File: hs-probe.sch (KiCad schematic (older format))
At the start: 52 parts, among them J1 USB_C_Receptacle_USB2.0, J2 Castellated Vias, J3 Castellated Vias, J4 Castellated Vias, U1 STM32F723IEKx, U2 DSC6003HI2A-012.0000T, U3 MIC5259, U4 NUF8401MNT4G, U5 STDC14, U6 SOICbite_SWD, U7 MIC5259, U8 USB3740B-AI9

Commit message: Updated design from review comment
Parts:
- added R9: 1k, passive:R_0402, symbol Device:R_Small
- J4: footprint connectors:1x4_1.5mm_castellated -> connectors:1x3_1.5mm_castellated; symbol Connector:Conn_01x04_Female -> Connector:Conn_01x03_Female
- U3, U7: value MIC5259 -> MIC5353; footprint dfn:DFN-6-1EP_2x2mm_P0.65mm_EP1x1.6mm -> dfn:DFN-6-1EP_1.6x1.6mm_P0.5mm_EP0.5x1.26mm; MPN MIC5259-3.3YML-TR -> MIC5353-3.3YMT
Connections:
- net labels added: FS_VBUS, HS_VBUS
- net labels removed: T_VCC_PWR
- wire segments 239 -> 246
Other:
- note added: "DESIGN NOTE:\nT_VCC is read before \nenabling 3.3V power."
- note removed: "DESIGN NOTE:\nT_VCC is not read, this assumes\nthat the target is running at the\nsame voltage as the probe."
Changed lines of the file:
@@
 	10000 1050 10000 650
 Text Notes 14200 1150 0    50   ~ 0
-DESIGN NOTE:\nT_VCC is not read, this assumes\nthat the target is running at the\nsame voltage as the probe.
+DESIGN NOTE:\nT_VCC is read before \nenabling 3.3V power.
 Wire Notes Line
-	14150 750  15500 750
+	14150 850  15050 850
 Wire Notes Line
-	15500 750  15500 1200
+	15050 850  15050 1200
 Wire Notes Line
-	15500 1200 14150 1200
+	15050 1200 14150 1200
 Wire Notes Line
-	14150 1200 14150 750
+	14150 1200 14150 850
 Text Label 14100 3650 2    50   ~ 0
 NRST
@@
 P 13000 7750
 F 0 "U3" H 13250 7915 50  0000 C CNN
-F 1 "MIC5259" H 13250 7824 50  0000 C CNN
-F 2 "dfn:DFN-6-1EP_2x2mm_P0.65mm_EP1x1.6mm" H 13000 7750 50  0001 C CNN
-F 3 "http://ww1.microchip.com/downloads/en/DeviceDoc/mic5259.pdf" H 13000 7750 50  0001 C CNN
-F 4 "MIC5259-3.3YML-TR" H 13000 7750 50  0001 C CNN "MPN"
+F 1 "MIC5353" H 13250 7824 50  0000 C CNN
+F 2 "dfn:DFN-6-1EP_1.6x1.6mm_P0.5mm_EP0.5x1.26mm" H 13000 7750 50  0001 C CNN
+F 3 "https://ww1.microchip.com/downloads/en/DeviceDoc/mic5353.pdf" H 13000 7750 50  0001 C CNN
+F 4 "MIC5353-3.3YMT" H 13000 7750 50  0001 C CNN "MPN"
 	1    13000 7750
 	1    0    0    -1
@@
 P 13000 8500
 F 0 "U7" H 13250 8665 50  0000 C CNN
-F 1 "MIC5259" H 13250 8574 50  0000 C CNN
-F 2 "dfn:DFN-6-1EP_2x2mm_P0.65mm_EP1x1.6mm" H 13000 8500 50  0001 C CNN
-F 3 "http://ww1.microchip.com/downloads/en/DeviceDoc/mic5259.pdf" H 13000 8500 50  0001 C CNN
-F 4 "MIC5259-3.3YML-TR" H 13000 8500 50  0001 C CNN "MPN"
+F 1 "MIC5353" H 13250 8574 50  0000 C CNN
+F 2 "dfn:DFN-6-1EP_1.6x1.6mm_P0.5mm_EP0.5x1.26mm" H 13000 8500 50  0001 C CNN
+F 3 "https://ww1.microchip.com/downloads/en/DeviceDoc/mic5353.pdf" H 13000 8500 50  0001 C CNN
+F 4 "MIC5353-3.3YMT" H 13000 8500 50  0001 C CNN "MPN"
 	1    13000 8500
 	1    0    0    -1
@@
 T_VCC_EN
 Text Label 14050 8600 0    50   ~ 0
-T_VCC_PWR
+T_VCC
 Text Label 13050 1100 2    50   ~ 0
 T_VCC
@@
 	7900 8700 7800 8700
 Text Label 13050 1000 2    50   ~ 0
-T_VCC_PWR
+T_VCC
 Wire Wire Line
 	13050 1000 13150 1000
@@
 $EndComp
 $Comp
-L Connector:Conn_01x04_Female J4
+L Connector:Conn_01x03_Female J4
 U 1 1 5F14F2FD
 P 13700 6000
-F 0 "J4" H 13592 5575 50  0000 C CNN
-F 1 "Castellated Vias" H 13592 5666 50  0000 C CNN
-F 2 "connectors:1x4_1.5mm_castellated" H 13700 6000 50  0001 C CNN
+F 0 "J4" H 13592 5675 50  0000 C CNN
+F 1 "Castellated Vias" H 13592 5766 50  0000 C CNN
+F 2 "connectors:1x3_1.5mm_castellated" H 13700 6000 50  0001 C CNN
 F 3 "~" H 13700 6000 50  0001 C CNN
 	1    13700 6000
@@
 Text Label 13400 4600 2    50   ~ 0
 T_TDI
-Text Label 13400 5800 2    50   ~ 0
-T_VCC
 Wire Wire Line
 	13400 5900 13500 5900
 Text Label 13400 5900 2    50   ~ 0
-T_VCC_PWR
-Wire Wire Line
-	13400 5800 13500 5800
+T_VCC
 Wire Wire Line
 	13400 5350 13500 5350
@@
 Wire Wire Line
 	7900 8000 7800 8000
+Text Label 7900 2800 0    50   ~ 0
+FS_VBUS
+Wire Wire Line
+	7900 2800 7800 2800
+Text Label 7900 4900 0    50   ~ 0
+HS_VBUS
+Wire Wire Line
+	7900 4900 7800 4900
+$Comp
+L Device:R_Small R9
+U 1 1 5F1A949A
+P 9600 2850
+F 0 "R9" V 9404 2850 50  0000 C CNN
+F 1 "1k" V 9495 2850 50  0000 C CNN
+F 2 "passive:R_0402" H 9600 2850 50  0001 C CNN
+F 3 "~" H 9600 2850 50  0001 C CNN
+F 4 "1%" H 9600 2850 50  0001 C CNN "Tolerance"
+	1    9600 2850
+	0    1    1    0
+$EndComp
+$Comp
+L power:+5V #PWR038
+U 1 1 5F1A9A32
+P 9850 2850
+F 0 "#PWR038" H 9850 2700 50  0001 C CNN
+F 1 "+5V" H 9865 3023 50  0000 C CNN
+F 2 "" H 9850 2850 50  0001 C CNN
+F 3 "" H 9850 2850 50  0001 C CNN
+	1    9850 2850
+	0    1    1    0
+$EndComp
+Wire Wire Line
+	9850 2850 9700 2850
+Wire Wire Line
+	9500 2850 9400 2850
+Wire Wire Line
+	9400 2850 9400 2750
+Wire Wire Line
+	9400 2750 9300 2750
+Wire Wire Line
+	9400 2950 9300 2950
+Wire Wire Line
+	9400 2850 9400 2950
+Connection ~ 9400 2850
+Text Label 9300 2750 2    50   ~ 0
+FS_VBUS
+Text Label 9300 2950 2    50   ~ 0
+HS_VBUS
 $EndSCHEMATC

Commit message: Major schematic cleanup
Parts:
- removed U1: STM32F723IEKx, bga:UFBGA-201_10x10mm_Layout15x15_P0.65mm, symbol MCU_ST_STM32F7:STM32F723IEKx
- added U1: hs-probe-stm32, bga:UFBGA-201_10x10mm_Layout15x15_P0.65mm, symbol hs-probe-stm32:hs-probe-stm32
- U2: value DSC6003HI2A-012.0000T -> 12 MHz
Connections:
- net +3V3: now also U1.C1 (VBAT), U1.C5 (VDD[12]), U1.C6 (PDR_ON), U1.C7 (VDD[12]), U1.C8 (VDDSDMMC), U1.C9 (VDD[12]), U1.F3 (VDD[12]), U1.G13 (VDD[12]), U1.G3 (VDD[12]), U1.H13 (VDDUSB), U1.J12 (VDD[12]), U1.J13 (VDD[12]), U1.K4 (VDD[12]), U1.N10 (VDD[12]), U1.N8 (VDD[12]), U1.N9 (VDD[12]), U1.P1 (VREF+), U1.R1 (VDDA)
- net BOOT0: now also U1.D6 (BOOT0)
- net D_FS_N: now also U1.C15 (PA11/USB_OTG_FS_DM)
- net D_FS_P: now also U1.B15 (PA12/USB_OTG_FS_DP)
- net D_HS_N: now also U1.R14 (PB14/USB_OTG_HS_DM)
- net D_HS_P: now also U1.R15 (PB15/USB_OTG_HS_DP)
- net FS_VBUS: now also U1.E15 (PA9/USB_OTG_FS_VBUS), U1.P13 (PB13/USB_OTG_HS_VBUS)
- net GND: now also U1.D5 (VSS[36]), U1.D7 (VSS[36]), U1.D8 (VSS[36]), U1.D9 (VSS[36]), U1.F10 (VSS[36]), U1.F12 (VSS[36]), U1.F2 (VSS[36]), U1.F6 (VSS[36]), U1.F7 (VSS[36]), U1.F8 (VSS[36]), U1.F9 (VSS[36]), U1.G10 (VSS[36]), U1.G12 (VSS[36]), U1.G2 (VSS[36]), U1.G6 (VSS[36]), U1.G7 (VSS[36]), U1.G8 (VSS[36]), U1.G9 (VSS[36]), U1.H10 (VSS[36]), U1.H12 (VSS[36]), U1.H6 (VSS[36]), U1.H7 (VSS[36]), U1.H8 (VSS[36]), U1.H9 (VSS[36]), U1.J10 (VSS[36]), U1.J6 (VSS[36]), U1.J7 (VSS[36]), U1.J8 (VSS[36]), U1.J9 (VSS[36]), U1.K10 (VSS[36]), U1.K6 (VSS[36]), U1.K7 (VSS[36]), U1.K8 (VSS[36]), U1.K9 (VSS[36]), U1.L4 (BYPASS_REG), U1.M1 (VSSA), U1.M8 (VSS[36]), U1.M9 (VSS[36]), U1.N1 (VREF-)
- net GNDDetect: now also U1.A7 (PG14/GNDDet)
- net GPIO1: now also U1.P15 (PD8/GPIO1)
- net GPIO2: now also U1.N15 (PD10/GPIO2)
- net LED1: now also U1.B14 (PC10/LED1)
- net LED2: now also U1.A5 (PB8/LED2)
- net LED3: now also U1.A4 (PE0/LED3)
- net NRST: now also U1.J1 (NRST)
- net OSC: now also U1.G1 (PH0-OSC_IN/RCC_OSC_IN)
- net P_SWCLK: now also U1.A14 (PA14/SYS_JTCK-SWCLK)
- net P_SWDIO: now also U1.A15 (PA13/SYS_JTMS-SWDIO)
- net RESET: now also U1.A8 (PG13/RESET)
- net RPHY: now also U1.J15 (REXTPHYHS)
- net SPI1_CLK: now also U1.A10 (PB3/SPI1_SCK), U1.D14 (PI1/SPI2_SCK)
- net SPI1_MISO: now also U1.A6 (PB5/SPI1_MOSI), U1.A9 (PB4/SPI1_MISO)
- net SPI2_MISO: now also U1.B5 (PB7/USART1_RX), U1.C14 (PI2/SPI2_MISO)
- net SPI2_MOSI: now also U1.C13 (PI3/SPI2_MOSI)
- net T_VCC_EN: now also U1.A2 (PE2/T_VCC_EN)
- net T_VCC_MEAS: now also U1.R2 (PA3/ADC1_IN3)
- net USART1_TX: now also U1.B6 (PB6/USART1_TX)
- net USART2_RX: now also U1.B11 (PD6/USART2_RX)
- net USART2_TX: now also U1.C11 (PD5/USART2_TX)
- net USB_SEL: now also U1.R12 (PB10/USB_SEL)
- net V12PHY: now also U1.J14 (V12PHYHS)
- net VCAP1: now also U1.M10 (VCAP_1)
- net VCAP2: now also U1.F13 (VCAP_2)
- no-connect marks 7 -> 86
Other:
- note added: "Board-edge castellated vias"
- note added: "DESIGN NOTE:\nOn startup the FS port is connected for access to the \nSTM32 USB bootloader. The firmware can then switch \nover to the HS port."
- note added: "Designed by: Emil Fresk\nTwitter / Github: @korken89\nLink: https://github.com/korken89/hs-probe"
- note added: "MCU I/O"
- note added: "MCU Power, Config and Clock"
- note added: "Probe power and optional target power"
- note added: "Target SWD/JTAG port with ESD protection"
- note added: "USB-C port with USB MUX"
- moved on the sheet: C1, C10, C11, C12, C13, C14, C15, C16, C17, C18, C19, C2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

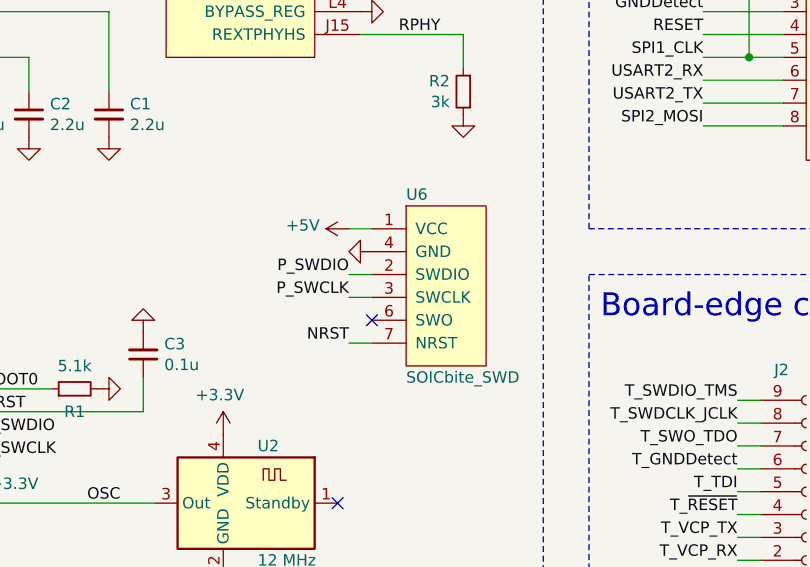
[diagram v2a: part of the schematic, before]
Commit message: Moved to tag connect
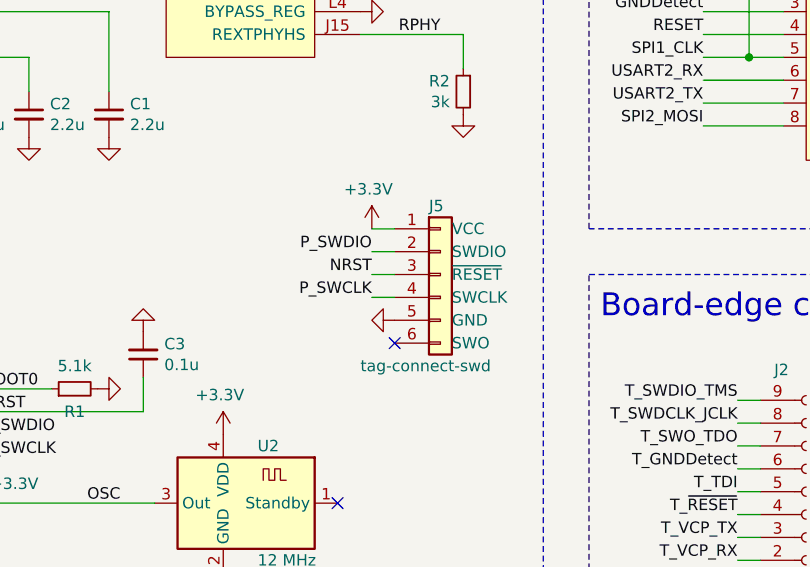
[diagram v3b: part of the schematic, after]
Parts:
- removed U6: SOICbite_SWD, connectors:SOICbiteSmall, symbol connectors:SOICbite_SWD
- added J5: tag-connect-swd, Connector:Tag-Connect_TC2030-IDC-NL_2x03_P1.27mm_Vertical, symbol connectors:tag-connect-swd
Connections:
- net +3V3: now also J5.1 (VCC)
- net GND: now also J5.5 (GND)
- net NRST: now also J5.3 (~RESET)
- net P_SWCLK: now also J5.4 (SWCLK)
- net P_SWDIO: now also J5.2 (SWDIO)
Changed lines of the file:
@@
 	3150 3750 3150 3600
 Wire Wire Line
-	4050 3450 4150 3450
-$Comp
-L connectors:SOICbite_SWD U6
-U 1 1 5EFB31C8
-P 4300 2850
-F 0 "U6" H 4300 2900 50  0000 L CNN
-F 1 "SOICbite_SWD" H 4300 2100 50  0000 L CNN
-F 2 "connectors:SOICbiteSmall" H 4300 2850 50  0001 C CNN
-F 3 "https://github.com/SimonMerrett/SOICbite" H 4300 2850 50  0001 C CNN
-	1    4300 2850
-	1    0    0    -1
-$EndComp
-Text Label 4050 3450 2    50   ~ 0
+	4150 3150 4250 3150
+Text Label 4150 3150 2    50   ~ 0
 NRST
-NoConn ~ 4150 3350
+NoConn ~ 4250 3450
 $Comp
 L power:GND #PWR0102
 U 1 1 5F023F3F
-P 4150 3050
-F 0 "#PWR0102" H 4150 2800 50  0001 C CNN
-F 1 "GND" H 4155 2877 50  0001 C CNN
-F 2 "" H 4150 3050 50  0001 C CNN
-F 3 "" H 4150 3050 50  0001 C CNN
-	1    4150 3050
+P 4250 3350
+F 0 "#PWR0102" H 4250 3100 50  0001 C CNN
+F 1 "GND" H 4255 3177 50  0001 C CNN
+F 2 "" H 4250 3350 50  0001 C CNN
+F 3 "" H 4250 3350 50  0001 C CNN
+	1    4250 3350
 	0    1    1    0
 $EndComp
 Wire Wire Line
-	4050 2950 4150 2950
-$Comp
-L power:+5V #PWR0101
-U 1 1 5F016F94
-P 4050 2950
-F 0 "#PWR0101" H 4050 2800 50  0001 C CNN
-F 1 "+5V" V 4065 3078 50  0000 L CNN
-F 2 "" H 4050 2950 50  0001 C CNN
-F 3 "" H 4050 2950 50  0001 C CNN
-	1    4050 2950
-	0    -1   -1   0
-$EndComp
-Wire Wire Line
-	4050 3150 4150 3150
-Wire Wire Line
-	4050 3250 4150 3250
-Text Label 4050 3250 2    50   ~ 0
+	4150 2950 4250 2950
+Wire Wire Line
+	4150 3050 4250 3050
+Wire Wire Line
+	4150 3250 4250 3250
+Text Label 4150 3250 2    50   ~ 0
 P_SWCLK
-Text Label 4050 3150 2    50   ~ 0
+Text Label 4150 3050 2    50   ~ 0
 P_SWDIO
 Wire Wire Line
@@
 NoConn ~ 5550 6500
 NoConn ~ 5550 6600
+$Comp
+L connectors:tag-connect-swd J5
+U 1 1 612A596E
+P 4450 3150
+F 0 "J5" H 4400 3450 50  0000 L CNN
+F 1 "tag-connect-swd" H 4100 2750 50  0000 L CNN
+F 2 "Connector:Tag-Connect_TC2030-IDC-NL_2x03_P1.27mm_Vertical" H 4450 3550 50  0001 C CNN
+F 3 "~" H 4450 3150 50  0001 C CNN
+	1    4450 3150
+	1    0    0    -1
+$EndComp
+$Comp
+L power:+3.3V #PWR0101
+U 1 1 6132BC89
+P 4150 2950
+F 0 "#PWR0101" H 4150 2800 50  0001 C CNN
+F 1 "+3.3V" H 4165 3123 50  0000 C CNN
+F 2 "" H 4150 2950 50  0001 C CNN
+F 3 "" H 4150 2950 50  0001 C CNN
+	1    4150 2950
+	-1   0    0    -1
+$EndComp
 $EndSCHEMATC

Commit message: Fixed ERC warnings
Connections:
- no-connect marks 86 -> 87
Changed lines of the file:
@@
 L power:+5V #PWR024
 U 1 1 5E947B8E
-P 8850 9000
-F 0 "#PWR024" H 8850 8850 50  0001 C CNN
-F 1 "+5V" H 8865 9173 50  0000 C CNN
-F 2 "" H 8850 9000 50  0001 C CNN
-F 3 "" H 8850 9000 50  0001 C CNN
-	1    8850 9000
+P 8600 8950
+F 0 "#PWR024" H 8600 8800 50  0001 C CNN
+F 1 "+5V" H 8615 9123 50  0000 C CNN
+F 2 "" H 8600 8950 50  0001 C CNN
+F 3 "" H 8600 8950 50  0001 C CNN
+	1    8600 8950
 	1    0    0    -1
 $EndComp
@@
 	8900 9050 8850 9050
 Wire Wire Line
-	8850 9050 8850 9000
+	8600 9050 8600 8950
 $Comp
 L power:+5V #PWR025
@@
 $EndComp
 Wire Wire Line
-	7100 6950 7550 6950
+	7100 6950 7200 6950
 Wire Wire Line
 	7650 7050 7550 7050
@@
 	-1   0    0    -1
 $EndComp
+NoConn ~ 2150 7900
+$Comp
+L power:PWR_FLAG #FLG0101
+U 1 1 6138C98D
+P 7200 6950
+F 0 "#FLG0101" H 7200 7025 50  0001 C CNN
+F 1 "PWR_FLAG" H 7200 7123 50  0000 C CNN
+F 2 "" H 7200 6950 50  0001 C CNN
+F 3 "~" H 7200 6950 50  0001 C CNN
+	1    7200 6950
+	1    0    0    -1
+$EndComp
+Connection ~ 7200 6950
+Wire Wire Line
+	7200 6950 7550 6950
+$Comp
+L power:PWR_FLAG #FLG0102
+U 1 1 613A98D8
+P 8850 9050
+F 0 "#FLG0102" H 8850 9125 50  0001 C CNN
+F 1 "PWR_FLAG" H 8850 9223 50  0000 C CNN
+F 2 "" H 8850 9050 50  0001 C CNN
+F 3 "~" H 8850 9050 50  0001 C CNN
+	1    8850 9050
+	1    0    0    -1
+$EndComp
+Connection ~ 8850 9050
+Wire Wire Line
+	8850 9050 8600 9050
+$Comp
+L power:PWR_FLAG #FLG0103
+U 1 1 613E4E60
+P 9400 10550
+F 0 "#FLG0103" H 9400 10625 50  0001 C CNN
+F 1 "PWR_FLAG" V 9400 10677 50  0000 L CNN
+F 2 "" H 9400 10550 50  0001 C CNN
+F 3 "~" H 9400 10550 50  0001 C CNN
+	1    9400 10550
+	0    -1   -1   0
+$EndComp
+Wire Wire Line
+	9400 10550 9500 10550
+Connection ~ 9500 10550
 $EndSCHEMATC

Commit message: Added license, dimensions and manufacturing specs
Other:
- note added: "LICENSE:\nThis work is licensed under CERN-OHL-P."
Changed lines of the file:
@@
 	9400 10550 9500 10550
 Connection ~ 9500 10550
+Text Notes 11900 9800 0    100  ~ 0
+LICENSE:\nThis work is licensed under CERN-OHL-P.
 $EndSCHEMATC

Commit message: Updated 3D models to FTSH-107-01-L-DV-K
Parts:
- U5: footprint connectors:PinHeader_2x07_P1.27mm_Vertical_SMD -> connectors:PinHeader_2x07_FTSH-107-01-L-DV-K
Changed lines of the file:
@@
 F 0 "U5" H 8550 1150 50  0000 L CNN
 F 1 "STDC14" H 9000 1150 50  0000 L CNN
-F 2 "connectors:PinHeader_2x07_P1.27mm_Vertical_SMD" H 8550 1100 50  0001 C CNN
+F 2 "connectors:PinHeader_2x07_FTSH-107-01-L-DV-K" H 8550 1100 50  0001 C CNN
 F 3 "" H 8550 1100 50  0001 C CNN
 F 4 "FTSH-107-01-L-DV-K" H 8550 1100 50  0001 C CNN "MPN"

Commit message: Improved ESD protection + current limiting clarity
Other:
- note added: "ESD protection + 100 ohm current limiting chip"
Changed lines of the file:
@@
 Text Notes 11900 9800 0    100  ~ 0
 LICENSE:\nThis work is licensed under CERN-OHL-P.
+Text Notes 5300 2800 0    50   ~ 0
+ESD protection + 100 ohm current limiting chip
 $EndSCHEMATC

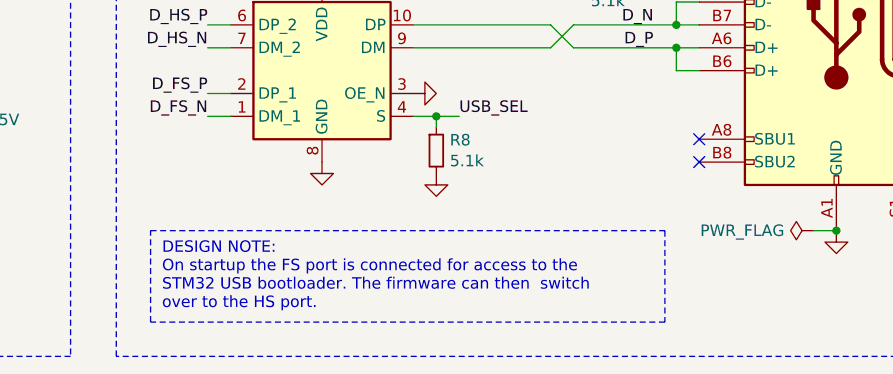
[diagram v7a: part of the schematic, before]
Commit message: Now using a 2x1.6mm crystal
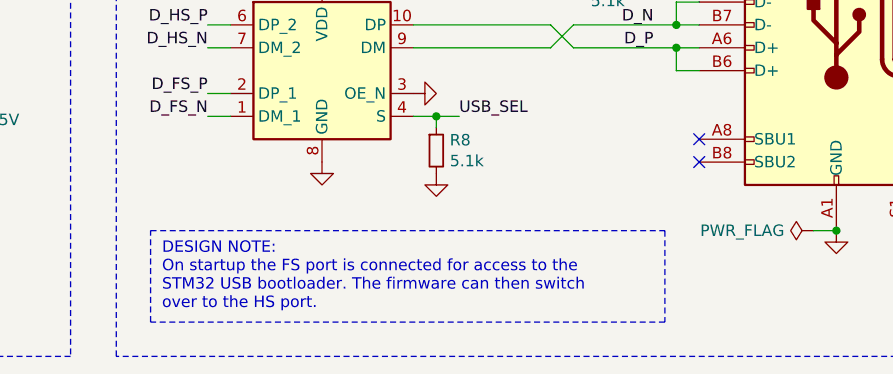
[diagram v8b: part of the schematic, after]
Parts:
- U2: footprint crystals:Oscillator_SMD_Abracon_ASCO-4Pin_1.6x1.2mm -> crystals:Crystal_4Pin_2.0x1.6mm; MPN DSC6003HI2A-012.0000T -> KC2016Z12.0000C15XXK
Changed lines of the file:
@@
 	6350 11100 6350 8500
 Text Notes 6550 10900 0    50   ~ 0
-DESIGN NOTE:\nOn startup the FS port is connected for access to the \nSTM32 USB bootloader. The firmware can then  switch \nover to the HS port.
+DESIGN NOTE:\nOn startup the FS port is connected for access to the \nSTM32 USB bootloader. The firmware can then switch \nover to the HS port.
 Wire Notes Line
 	6500 10550 8750 10550
@@
 F 0 "U2" H 3550 4400 50  0000 R CNN
 F 1 "12 MHz" H 3550 3900 50  0000 R CNN
-F 2 "crystals:Oscillator_SMD_Abracon_ASCO-4Pin_1.6x1.2mm" H 3600 4150 50  0001 C CNN
-F 3 "http://ww1.microchip.com/downloads/en/DeviceDoc/DSC60XX-Ultra-Small-Ultra-Low-Power-MEMS-Oscillator-DS20005625C.pdf" H 3900 4600 50  0001 C CNN
-F 4 "DSC6003HI2A-012.0000T" H 3600 4150 50  0001 C CNN "MPN"
+F 2 "crystals:Crystal_4Pin_2.0x1.6mm" H 3600 4150 50  0001 C CNN
+F 3 "https://global.kyocera.com/prdct/electro/product/pdf/clock_z_xz_e.pdf" H 3900 4600 50  0001 C CNN
+F 4 "KC2016Z12.0000C15XXK" H 3600 4150 50  0001 C CNN "MPN"
 	1    3600 4150
 	-1   0    0    -1
